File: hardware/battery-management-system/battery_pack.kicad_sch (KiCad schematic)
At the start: 23 parts, among them J1 CELLS, J2 Charge, J3 Discharge, J4 VBAT_DISCHARGE, Q1 DMN3404L, Q2 TJ40S04M3L, Q3 TJ40S04M3L, Q4 DMN3404L, U11 STC3100

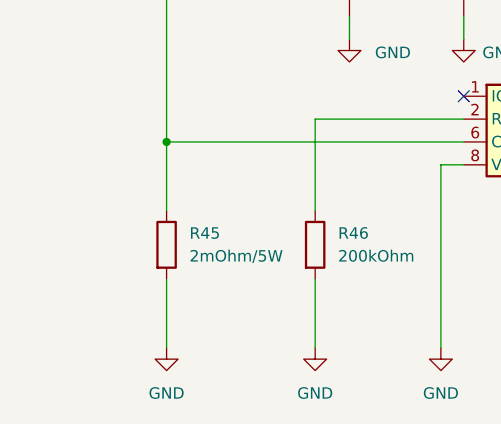
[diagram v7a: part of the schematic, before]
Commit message: add heatsink to sense resistor
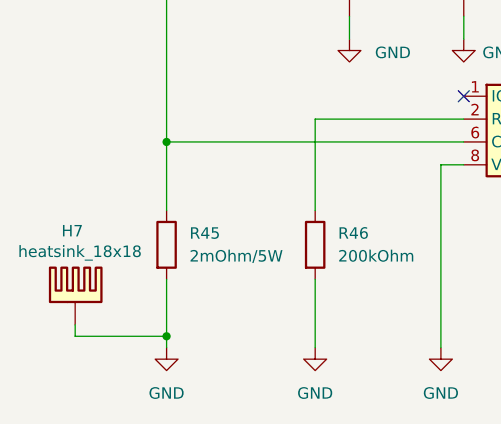
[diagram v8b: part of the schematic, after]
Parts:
- added H7: heatsink_18x18, benediktibk:heatsink_18x18, symbol benediktibk:heatsink_18x18
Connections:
- net GND: now also H7.PAD
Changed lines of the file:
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@@
 	(paper "A4")
+	(junction
+		(at 48.26 157.48)
+		(diameter 0)
+		(color 0 0 0 0)
+	)
 	(junction
 		(at 68.58 111.76)
@@
 	(wire
 		(pts
+			(xy 38.1 156.21) (xy 38.1 157.48)
+		)
+		(stroke
+			(width 0)
+			(type default)
+		)
+	)
+	(wire
+		(pts
 			(xy 81.28 133.35) (xy 64.77 133.35)
 		)
@@
 	(wire
 		(pts
+			(xy 38.1 157.48) (xy 48.26 157.48)
+		)
+		(stroke
+			(width 0)
+			(type default)
+		)
+	)
+	(wire
+		(pts
 			(xy 171.45 62.23) (xy 158.75 62.23)
 		)
@@
 	(wire
 		(pts
-			(xy 48.26 151.13) (xy 48.26 158.75)
+			(xy 48.26 151.13) (xy 48.26 157.48)
 		)
 		(stroke
@@
 		(pts
 			(xy 144.78 101.6) (xy 144.78 104.14)
+		)
+		(stroke
+			(width 0)
+			(type default)
+		)
+	)
+	(wire
+		(pts
+			(xy 48.26 157.48) (xy 48.26 158.75)
 		)
 		(stroke
@@
 					(unit 1)
 				)
+			)
+		)
+	)
+	(symbol
+		(lib_id "benediktibk:heatsink_18x18")
+		(at 38.1 152.4 0)
+		(unit 1)
+		(exclude_from_sim no)
+		(in_bom yes)
+		(on_board yes)
+		(dnp no)
+		(property "Reference" "H7"
+			(at 36.576 145.796 0)
+			(effects
+				(font
+					(size 1.27 1.27)
+				)
+				(justify left)
+			)
+		)
+		(property "Value" "heatsink_18x18"
+			(at 31.75 148.082 0)
+			(effects
+				(font
+					(size 1.27 1.27)
+				)
+				(justify left)
+			)
+		)
+		(property "Footprint" "benediktibk:heatsink_18x18"
+			(at 38.227 142.494 0)
+			(effects
+				(font
+					(size 1.27 1.27)
+				)
+				(hide yes)
+			)
+		)
+		(property "Datasheet" "~"
+			(at 38.1 144.78 0)
+			(effects
+				(font
+					(size 1.27 1.27)
+				)
+				(hide yes)
+			)
+		)
+		(property "Description" ""
+			(at 37.846 152.4 0)
+			(effects
+				(font
+					(size 1.27 1.27)
+				)
+				(hide yes)
+			)
+		)
+		(property "Mouser order number" "490-HSB06-181810"
+			(at 38.608 146.558 0)
+			(effects
+				(font
+					(size 1.27 1.27)
+				)
+				(hide yes)
+			)
+		)
+		(pin "PAD"
+		)
+		(instances
+			(project "battery-management-system"
+				(path "/5272f0ff-3069-41a9-bca2-80beede8b4b2/31b87c35-c096-4dc0-8978-834bec283b57"
+					(reference "H7")
+					(unit 1)
+				)
